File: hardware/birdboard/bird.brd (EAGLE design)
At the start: 73.7 x 68.6 mm, 39 parts, among them IC1 ATMEGA88-THIN

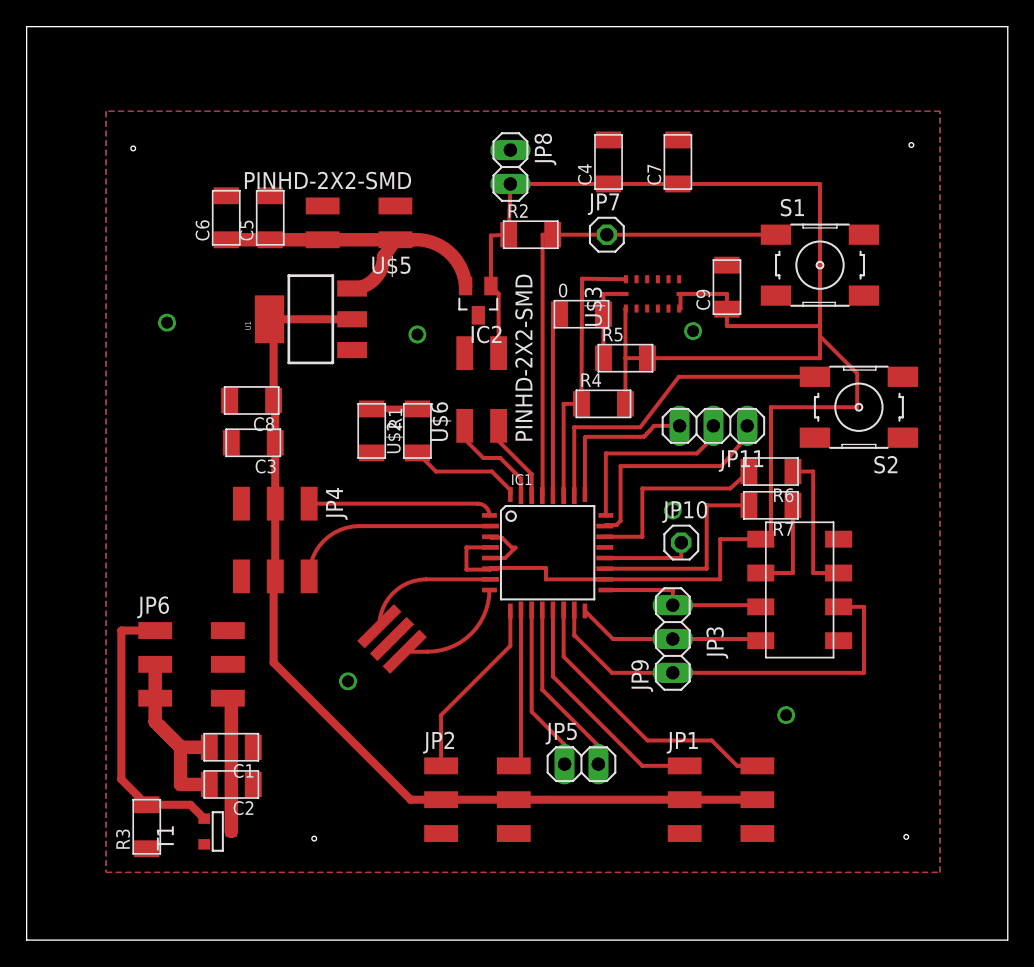
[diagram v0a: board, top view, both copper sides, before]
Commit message: Remove DigialIO since we don't need software implementations, updated bird board to newer version
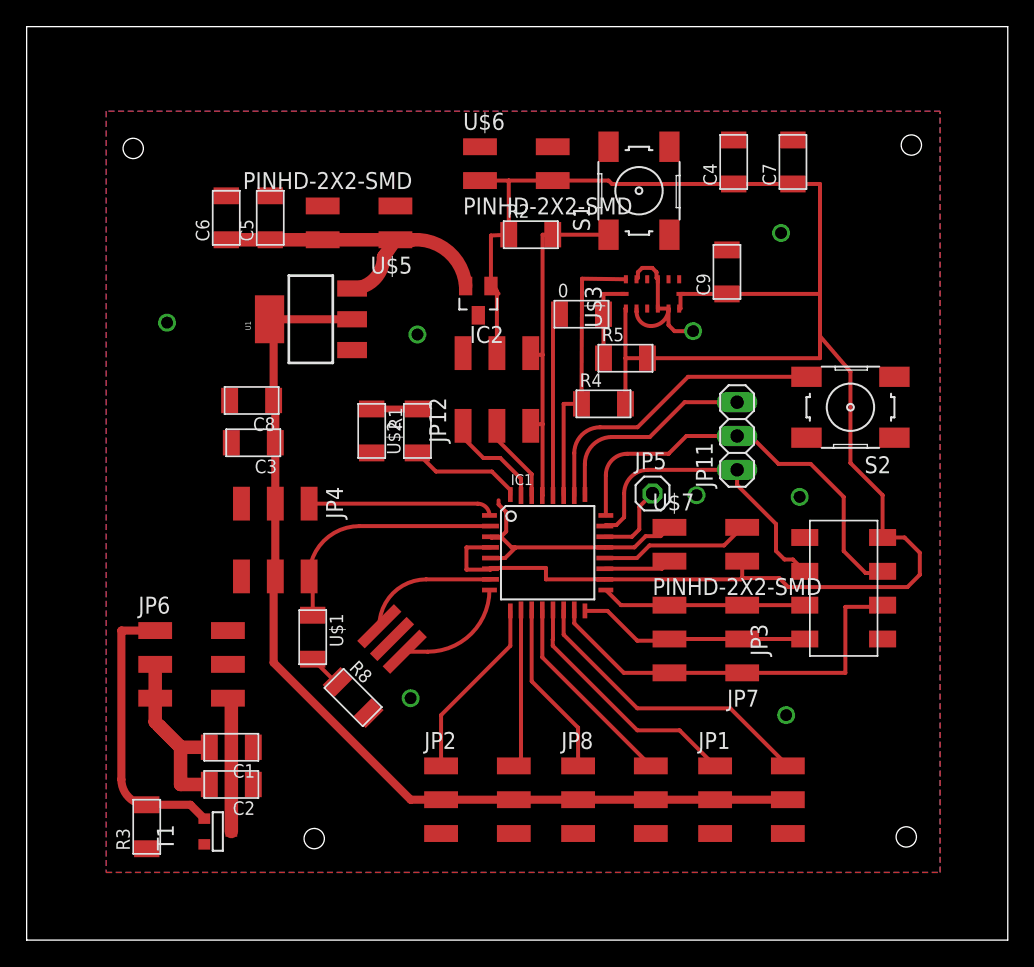
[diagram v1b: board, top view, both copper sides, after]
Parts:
- removed JP10: (no value), pinhead+:1X01
- removed JP9: (no value), pinhead+:1X03
- removed R6, R7: 0, fab:R1206FAB
- added JP12: (no value), fab:2X03SMD
- added R8: 1k, fab:R1206FAB
- added U$1: LEDFAB1206, fab:LED1206FAB
- added U$7: PINHD-2X2-SMD, fab:2X02SMD
- JP5: device pinhead:1X02 -> pinhead:1X01
- JP7: device pinhead+:1X01 -> fab:2X03SMD
- JP8: device pinhead:1X02 -> fab:2X03SMD
- R1: value (none) -> 1k
- moved JP8 48.1 mm to (43.9, 10.5), turned to 0 degrees
- moved JP7 31.3 mm to (51.2, 22.6), turned to 180 degrees
- moved JP5 21.0 mm to (47.0, 33.5)
- moved U$6 17.3 mm to (36.6, 58.3), turned to 0 degrees
- moved S1 14.7 mm to (46.0, 56.3), turned to 90 degrees
- moved C4 9.40 mm to (53.1, 58.4)
- moved C7 8.64 mm to (57.5, 58.4)
- moved JP3 3.30 mm to (61.3, 26.4)
- moved JP1 2.29 mm to (54.2, 10.5)
- moved JP11 1.93 mm to (53.3, 37.8), turned to 90 degrees
- moved C9 1.14 mm to (52.6, 50.2)
- moved S2 0.64 mm to (61.8, 40.0)
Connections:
- removed net CE0: IC1.19, R7.2
- removed net CSN0: IC1.22, R6.2
- removed net Y: IC1.24, JP11.2
- removed net Z: IC1.25, JP11.3
- new net ADC6: IC1.19, U$7.3
- new net ADC7: IC1.22, JP5.1
- new net N$3: R8.1, U$1.2
- net +5V: now also JP8.3, JP8.4
- net A: now also JP8.1; no longer JP5.1
- net AREF: now also U$7.2; no longer JP10.1
- net B: now also JP8.2; no longer JP5.2
- net CE: now also IC1.23, JP11.1; no longer R7.1
- net CSN: now also IC1.24, JP11.2; no longer R6.1
- net GND: now also JP12.2, JP3.8, JP8.5, JP8.6, R8.2, U$6.1, U$7.1; no longer JP3.7, JP8.1
- net MISO: now also JP7.3, JP7.4; no longer JP9.2
- net MOSI: now also JP7.1, JP7.2; no longer JP9.1
- net RESET: now also JP12.5, JP12.6; no longer JP7.1
- net RX: now also JP12.3; no longer U$6.3
- net SCK: now also JP7.5, JP7.6; no longer JP9.3
- net T0: now also U$1.1
- net TX: now also JP12.1; no longer U$6.1
- net VCC: now also JP12.4, JP3.7, U$6.3, U$7.4; no longer JP3.8, JP8.2
- net X: now also IC1.25, JP11.3; no longer IC1.23, JP11.1
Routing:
- net GND: track 4.42 -> 33.5 mm, vias 6 -> 8
- net CSN: track 11.0 -> 31.7 mm
- net CE0: track 15.6 -> 0.00 mm
- net CE: track 7.49 -> 22.8 mm
- net CSN0: track 14.9 -> 0.00 mm
- net Y: track 14.0 -> 0.00 mm
- net Z: track 11.8 -> 0.00 mm
- net RESET: track 37.3 -> 26.4 mm
- net VCC: track 139.9 -> 149.6 mm
- net ADC7: track 0.00 -> 5.92 mm
- net ADC6: track 0.00 -> 5.09 mm
- net AREF: track 6.90 -> 11.3 mm
- net +5V: track 73.8 -> 77.1 mm
- net MISO: track 14.2 -> 17.5 mm
- net T0: track 15.2 -> 18.2 mm
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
